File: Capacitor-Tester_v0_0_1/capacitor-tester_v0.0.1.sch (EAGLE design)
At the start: 32 parts, among them IC1 AD8531ARZ, IC2 MC34063EBD-TR, IC3 DAC6571IDBVT, IC4 AD8531ARZ, J1 USB4125-GF-A-0190_REVA2, J2 DS1044-140G, J4 250-103, U1 AD5933, U2 LM6171AIMX/NOPB, Y1 LFSPXO018034

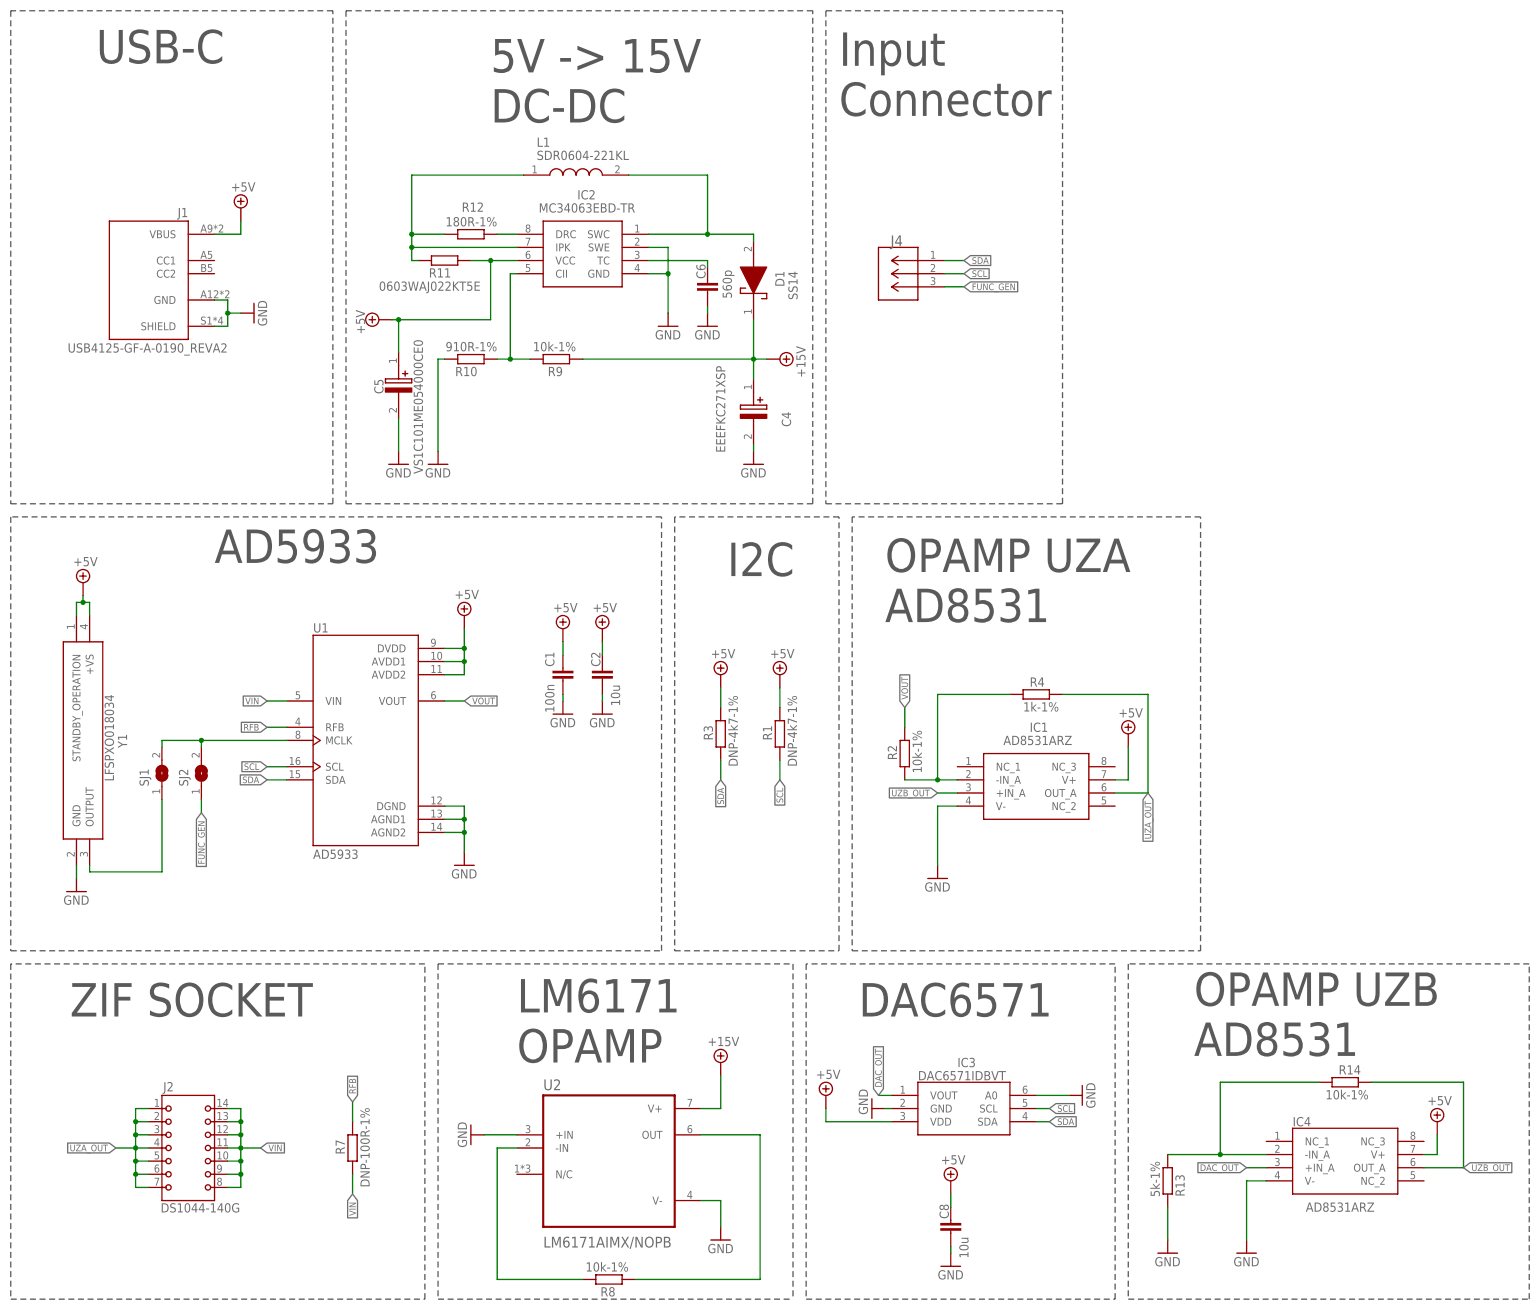
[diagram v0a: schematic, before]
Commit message: v0.0.1 - Changed both stages of the opamps. Need to change from 15V to 12V
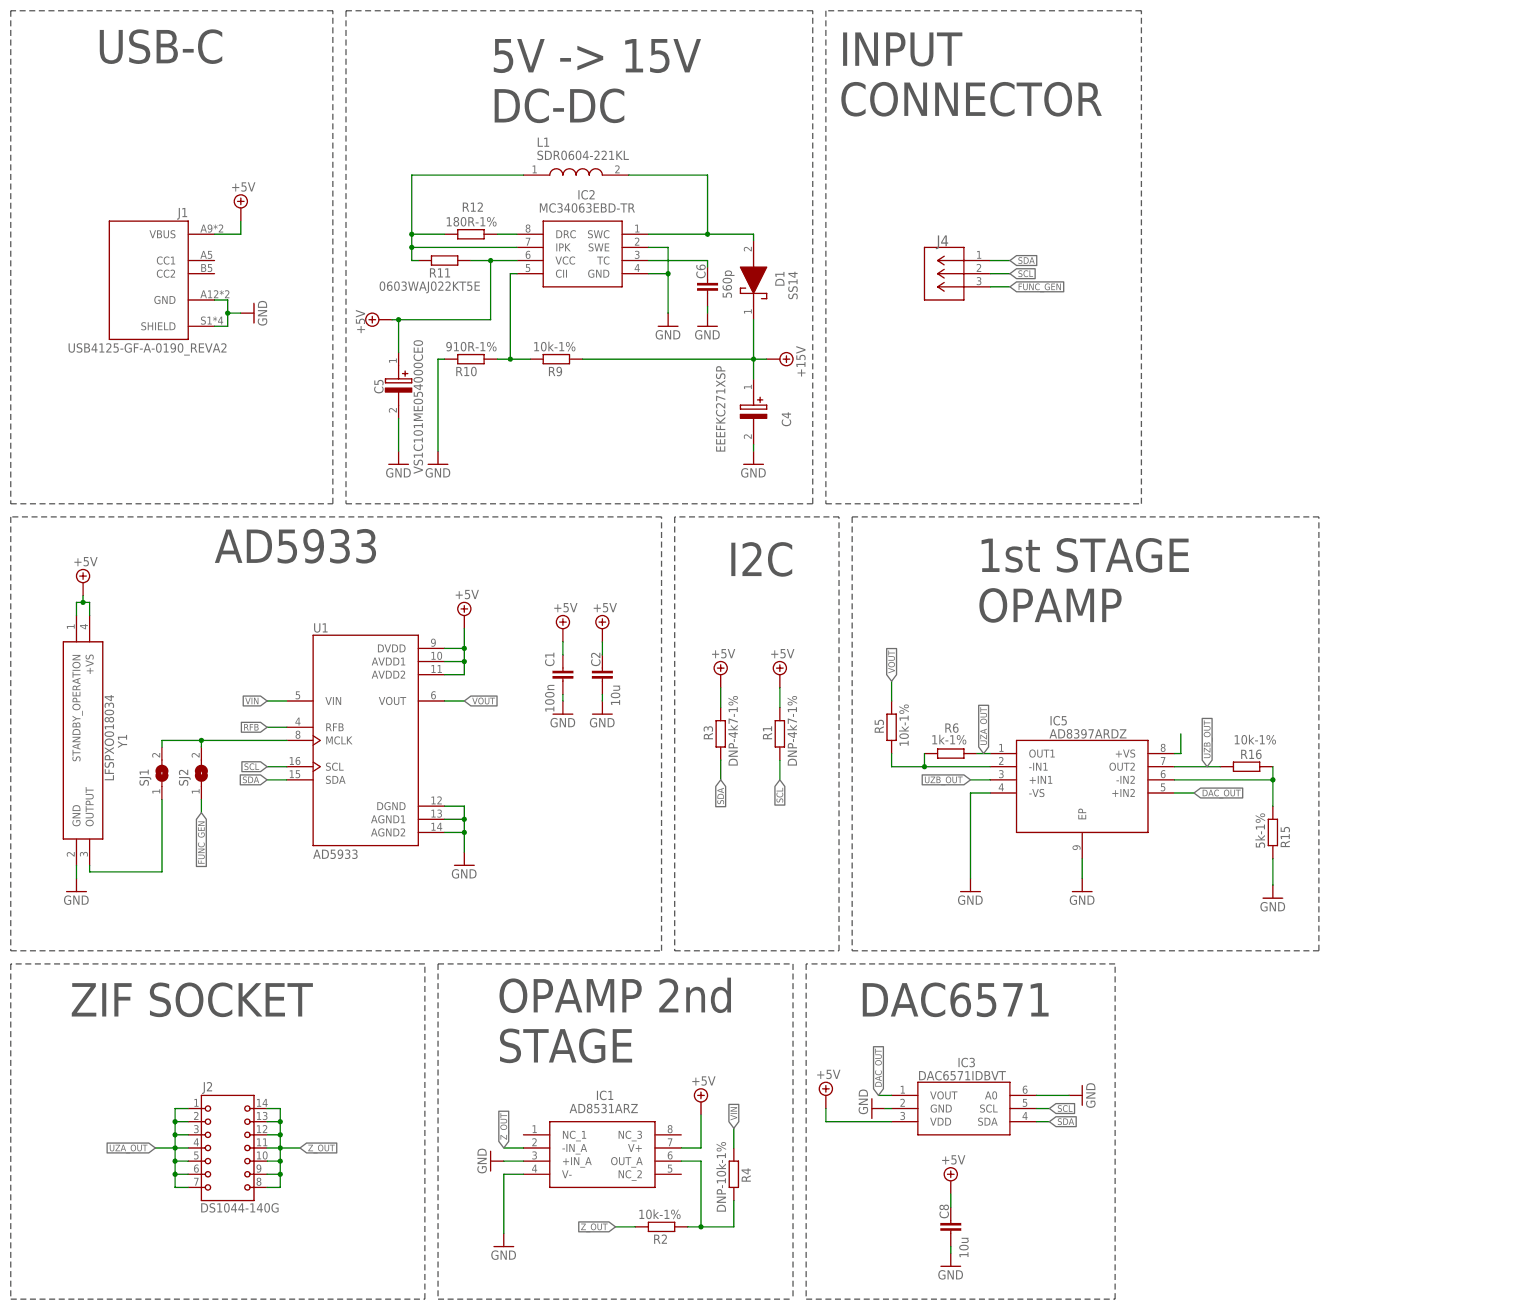
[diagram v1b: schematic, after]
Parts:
- removed IC4: AD8531ARZ, AD8531ARZ:AD8531ARZ
- removed R13: 5k-1%, custom_library:RESISTOR_SMD0603
- removed R14, R8: 10k-1%, custom_library:RESISTOR_SMD0603
- removed R7: DNP-100R-1%, custom_library:RESISTOR_SMD0603
- removed U2: LM6171AIMX/NOPB, LM6171AIMX_NOPB:LM6171AIMX/NOPB
- added IC5: AD8397ARDZ, AD8397ARDZ:AD8397ARDZ
- added R15: 5k-1%, custom_library:RESISTOR_SMD0603
- added R16, R5: 10k-1%, custom_library:RESISTOR_SMD0603
- added R6: 1k-1%, custom_library:RESISTOR_SMD0603
- R4: value 1k-1% -> DNP-10k-1%
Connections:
- removed net N$2: R8.2, U2.-IN
- removed net N$3: R8.1, U2.OUT
- removed net N$9: IC4.-IN_A, R13.1, R14.1
- new net N$12: IC5.+VS
- new net N$13: IC5.-IN2, R15.1, R16.2
- new net N$4: IC5.-IN1, R5.1, R6.1
- new net Z_OUT: IC1.-IN_A, J2.10, J2.11, J2.12, J2.13, J2.14, J2.8, J2.9, R2.2
- net +15V: no longer U2.V+
- net +5V: no longer IC4.V+
- net DAC_OUT: now also IC5.+IN2; no longer IC4.+IN_A
- net GND: now also IC1.+IN_A, IC5.-VS, IC5.EP, R15.2; no longer IC4.V-, R13.2, U2.+IN, U2.V-
- net N$1: now also IC1.OUT_A, R4.2; no longer IC1.-IN_A, R4.1
- net RFB: no longer R7.2
- net UZA_OUT: now also IC5.OUT1, R6.2; no longer IC1.OUT_A, R4.2
- net UZB_OUT: now also IC5.+IN1, IC5.OUT2, R16.1; no longer IC1.+IN_A, IC4.OUT_A, R14.2
- net VIN: now also R4.1; no longer J2.10, J2.11, J2.12, J2.13, J2.14, J2.8, J2.9, R7.1
- net VOUT: now also R5.2; no longer R2.2
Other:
- note added: "1st STAGE OPAMP"
- note added: "INPUT CONNECTOR"
- note added: "OPAMP 2nd STAGE"
- note removed: "Input Connector"
- note removed: "LM6171 OPAMP"
- note removed: "OPAMP UZA AD8531"
- note removed: "OPAMP UZB AD8531"
- moved on the sheet: IC1, J2, J4, R2, R4

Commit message: v0.0.1 - Changed boost converter to +12V on output and added shottky diode
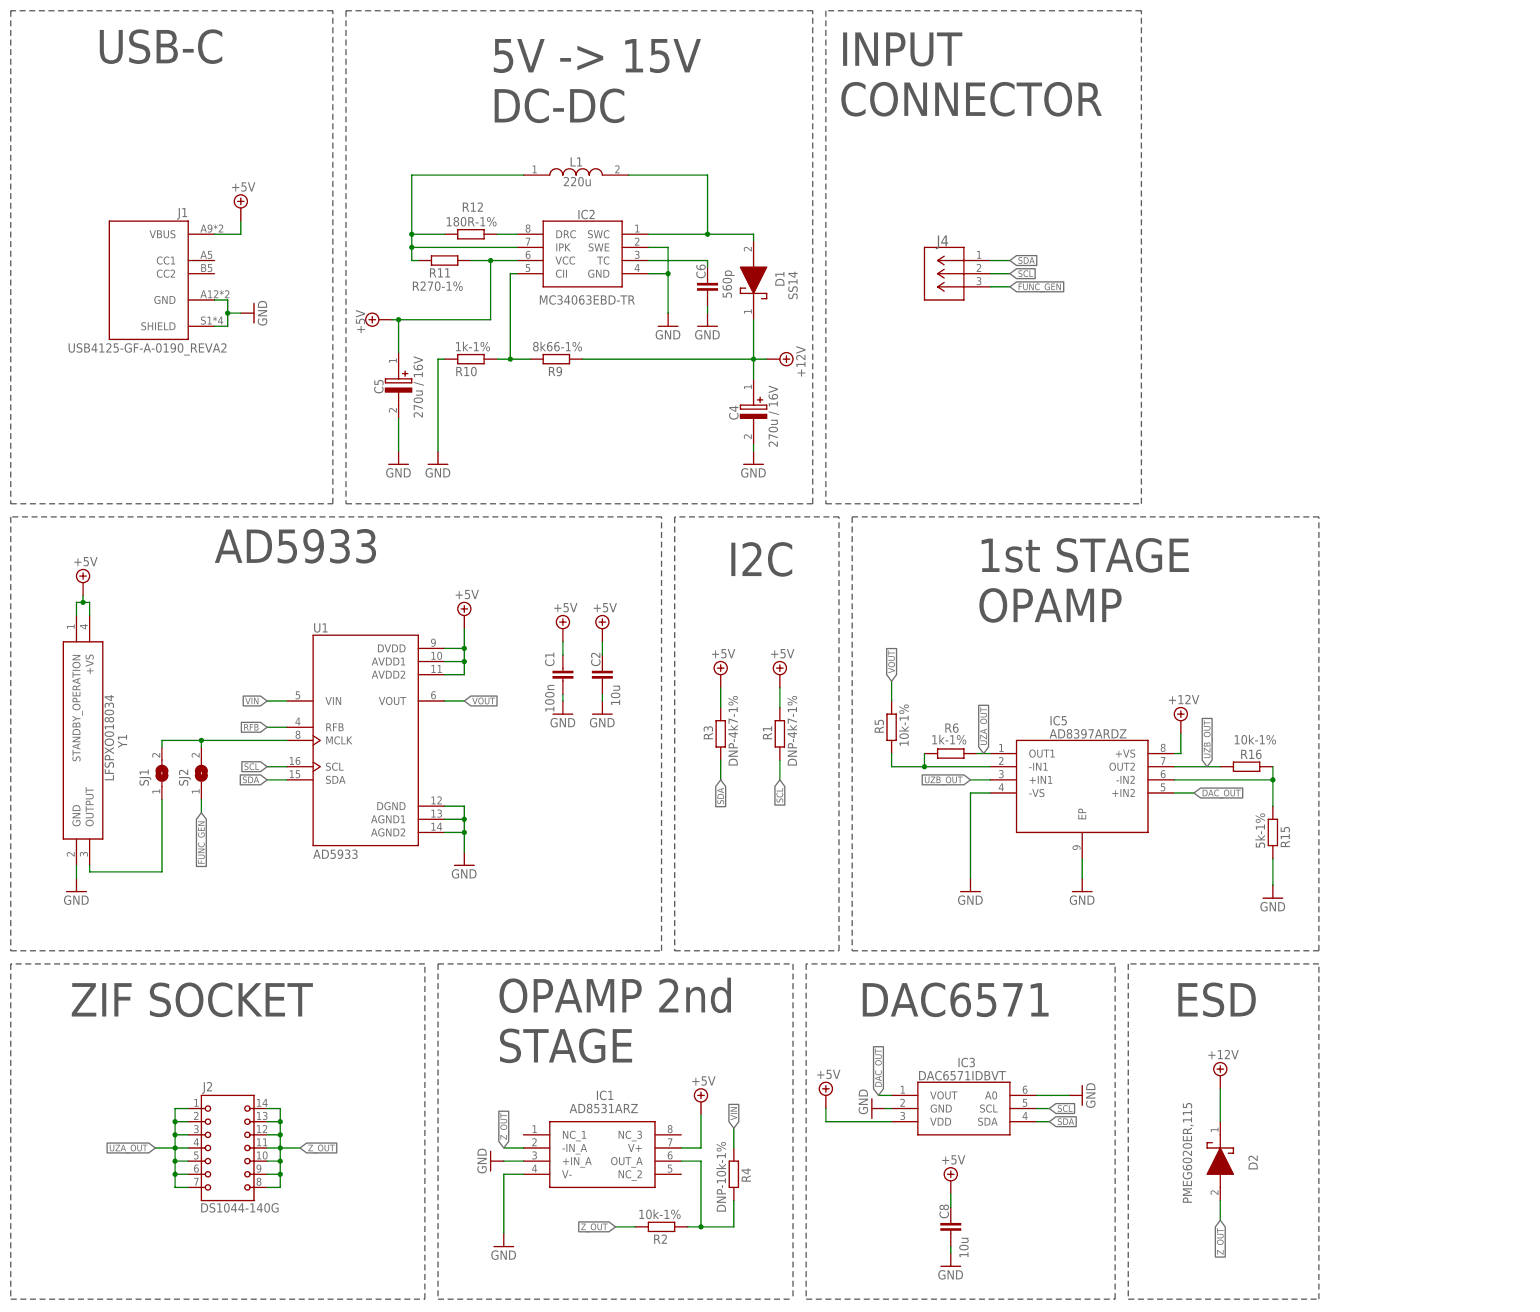
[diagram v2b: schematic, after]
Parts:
- added D2: PMEG6020ER,115, PMEG6020ER_115:PMEG6020ER,115
- C4: value EEEFKC271XSP -> 270u / 16V
- C5: value VS1C101ME054000CE0 -> 270u / 16V
- L1: value SDR0604-221KL -> 220u
- R10: value 910R-1% -> 1k-1%
- R11: value 0603WAJ022KT5E -> R270-1%
- R9: value 10k-1% -> 8k66-1%
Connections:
- removed net +15V: C4.+, D1.K, R9.1
- removed net N$12: IC5.+VS
- new net +12V: C4.+, D1.K, D2.K, IC5.+VS, R9.1
- net Z_OUT: now also D2.A
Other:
- note added: "ESD"

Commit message: v0.0.1 - Changed L1
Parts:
- L1: value 220u -> 15uH; device SDR0604-221KL:SDR0604-221KL -> SDR0604-150YL:SDR0604-150YL
- R11: value R270-1% -> R133-1%

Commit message: IN PROGRESS - arranging elements
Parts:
- added C3, C7: 100n, custom_library:CAPACITOR_SMD_CERAMIC0603
- R15: value 5k-1% -> 10k-1%
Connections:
- net +12V: now also C3.1; no longer D2.K
- net +5V: now also C7.1, D2.K
- net GND: now also C3.2, C7.2
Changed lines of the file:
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@@
 <part name="R5" library="custom_library" deviceset="RESISTOR_SMD" device="0603" value="10k-1%"/>
 <part name="R6" library="custom_library" deviceset="RESISTOR_SMD" device="0603" value="1k-1%"/>
-<part name="R15" library="custom_library" deviceset="RESISTOR_SMD" device="0603" value="5k-1%"/>
+<part name="R15" library="custom_library" deviceset="RESISTOR_SMD" device="0603" value="10k-1%"/>
 <part name="GND7" library="supply1" library_urn="urn:adsk.eagle:library:371" deviceset="GND" device=""/>
 <part name="R16" library="custom_library" deviceset="RESISTOR_SMD" device="0603" value="10k-1%"/>
@@
 <part name="SUPPLY10" library="supply2" library_urn="urn:adsk.eagle:library:372" deviceset="+12V" device=""/>
 <part name="D2" library="PMEG6020ER_115" deviceset="PMEG6020ER,115" device=""/>
-<part name="SUPPLY13" library="supply2" library_urn="urn:adsk.eagle:library:372" deviceset="+12V" device=""/>
 <part name="L1" library="SDR0604-150YL" deviceset="SDR0604-150YL" device="" value="15uH"/>
+<part name="C3" library="custom_library" deviceset="CAPACITOR_SMD_CERAMIC" device="0603" value="100n"/>
+<part name="GND9" library="supply1" library_urn="urn:adsk.eagle:library:371" deviceset="GND" device=""/>
+<part name="SUPPLY14" library="supply2" library_urn="urn:adsk.eagle:library:372" deviceset="+12V" device=""/>
+<part name="C7" library="custom_library" deviceset="CAPACITOR_SMD_CERAMIC" device="0603" value="100n"/>
+<part name="GND10" library="supply1" library_urn="urn:adsk.eagle:library:371" deviceset="GND" device=""/>
+<part name="SUPPLY15" library="supply2" library_urn="urn:adsk.eagle:library:372" deviceset="+5V" device=""/>
+<part name="SUPPLY13" library="supply2" library_urn="urn:adsk.eagle:library:372" deviceset="+5V" device=""/>
 </parts>
 <sheets>
@@
 <attribute name="VALUE" x="134.62" y="-44.45" size="1.778" layer="96" rot="R270" align="center-left"/>
 </instance>
-<instance part="SUPPLY13" gate="+12V" x="140.97" y="-39.37" smashed="yes">
-<attribute name="VALUE" x="138.43" y="-36.195" size="1.778" layer="96"/>
-</instance>
 <instance part="L1" gate="G$1" x="6.35" y="134.62" smashed="yes">
 <attribute name="NAME" x="15.24" y="137.16" size="1.778" layer="95" align="center-left"/>
 <attribute name="VALUE" x="13.97" y="133.35" size="1.778" layer="96" align="center-left"/>
+</instance>
+<instance part="C3" gate="G$1" x="153.67" y="40.64" smashed="yes">
+<attribute name="NAME" x="152.019" y="42.164" size="1.778" layer="95" rot="R90"/>
+<attribute name="VALUE" x="152.019" y="33.274" size="1.778" layer="96" rot="R90"/>
+</instance>
+<instance part="GND9" gate="1" x="153.67" y="33.02" smashed="yes">
+<attribute name="VALUE" x="151.13" y="30.48" size="1.778" layer="96"/>
+</instance>
+<instance part="SUPPLY14" gate="+12V" x="153.67" y="49.53" smashed="yes">
+<attribute name="VALUE" x="151.13" y="52.705" size="1.778" layer="96"/>
+</instance>
+<instance part="C7" gate="G$1" x="54.61" y="-60.96" smashed="yes">
+<attribute name="NAME" x="52.959" y="-59.436" size="1.778" layer="95" rot="R90"/>
+<attribute name="VALUE" x="52.959" y="-68.326" size="1.778" layer="96" rot="R90"/>
+</instance>
+<instance part="GND10" gate="1" x="54.61" y="-68.58" smashed="yes">
+<attribute name="VALUE" x="52.07" y="-71.12" size="1.778" layer="96"/>
+</instance>
+<instance part="SUPPLY15" gate="+5V" x="54.61" y="-52.07" smashed="yes">
+<attribute name="VALUE" x="52.705" y="-48.895" size="1.778" layer="96"/>
+</instance>
+<instance part="SUPPLY13" gate="+5V" x="140.97" y="-39.37" smashed="yes">
+<attribute name="VALUE" x="139.065" y="-36.195" size="1.778" layer="96"/>
 </instance>
 </instances>
@@
 <pinref part="GND19" gate="1" pin="GND"/>
 </segment>
+<segment>
+<pinref part="C3" gate="G$1" pin="2"/>
+<wire x1="153.67" y1="36.83" x2="153.67" y2="35.56" width="0.1524" layer="91"/>
+<pinref part="GND9" gate="1" pin="GND"/>
+</segment>
+<segment>
+<pinref part="C7" gate="G$1" pin="2"/>
+<wire x1="54.61" y1="-64.77" x2="54.61" y2="-66.04" width="0.1524" layer="91"/>
+<pinref part="GND10" gate="1" pin="GND"/>
+</segment>
 </net>
 <net name="+5V" class="0">
@@
 <wire x1="40.64" y1="-53.34" x2="40.64" y2="-46.99" width="0.1524" layer="91"/>
 <pinref part="SUPPLY8" gate="+5V" pin="+5V"/>
+</segment>
+<segment>
+<pinref part="C7" gate="G$1" pin="1"/>
+<wire x1="54.61" y1="-57.15" x2="54.61" y2="-54.61" width="0.1524" layer="91"/>
+<pinref part="SUPPLY15" gate="+5V" pin="+5V"/>
+</segment>
+<segment>
+<pinref part="D2" gate="G$1" pin="K"/>
+<wire x1="140.97" y1="-48.26" x2="140.97" y2="-41.91" width="0.1524" layer="91"/>
+<pinref part="SUPPLY13" gate="+5V" pin="+5V"/>
 </segment>
 </net>
@@
 </segment>
 <segment>
-<pinref part="D2" gate="G$1" pin="K"/>
-<wire x1="140.97" y1="-48.26" x2="140.97" y2="-41.91" width="0.1524" layer="91"/>
-<pinref part="SUPPLY13" gate="+12V" pin="+12V"/>
-</segment>
-</net>
+<pinref part="C3" gate="G$1" pin="1"/>
+<wire x1="153.67" y1="44.45" x2="153.67" y2="46.99" width="0.1524" layer="91"/>
+<pinref part="SUPPLY14" gate="+12V" pin="+12V"/>
+</segment>
+</net>
